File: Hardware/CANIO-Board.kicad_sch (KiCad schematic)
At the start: 52 parts, among them J1 DT13-2P, J2 Conn_01x04_Pin, J3 Conn_01x03_Pin, U1 STM32G0B1KETx, U2 AP63203WU-7, U3 AP63205WU-7, U4 ISOW1044, U5 TPS4H160AQPWPRQ1

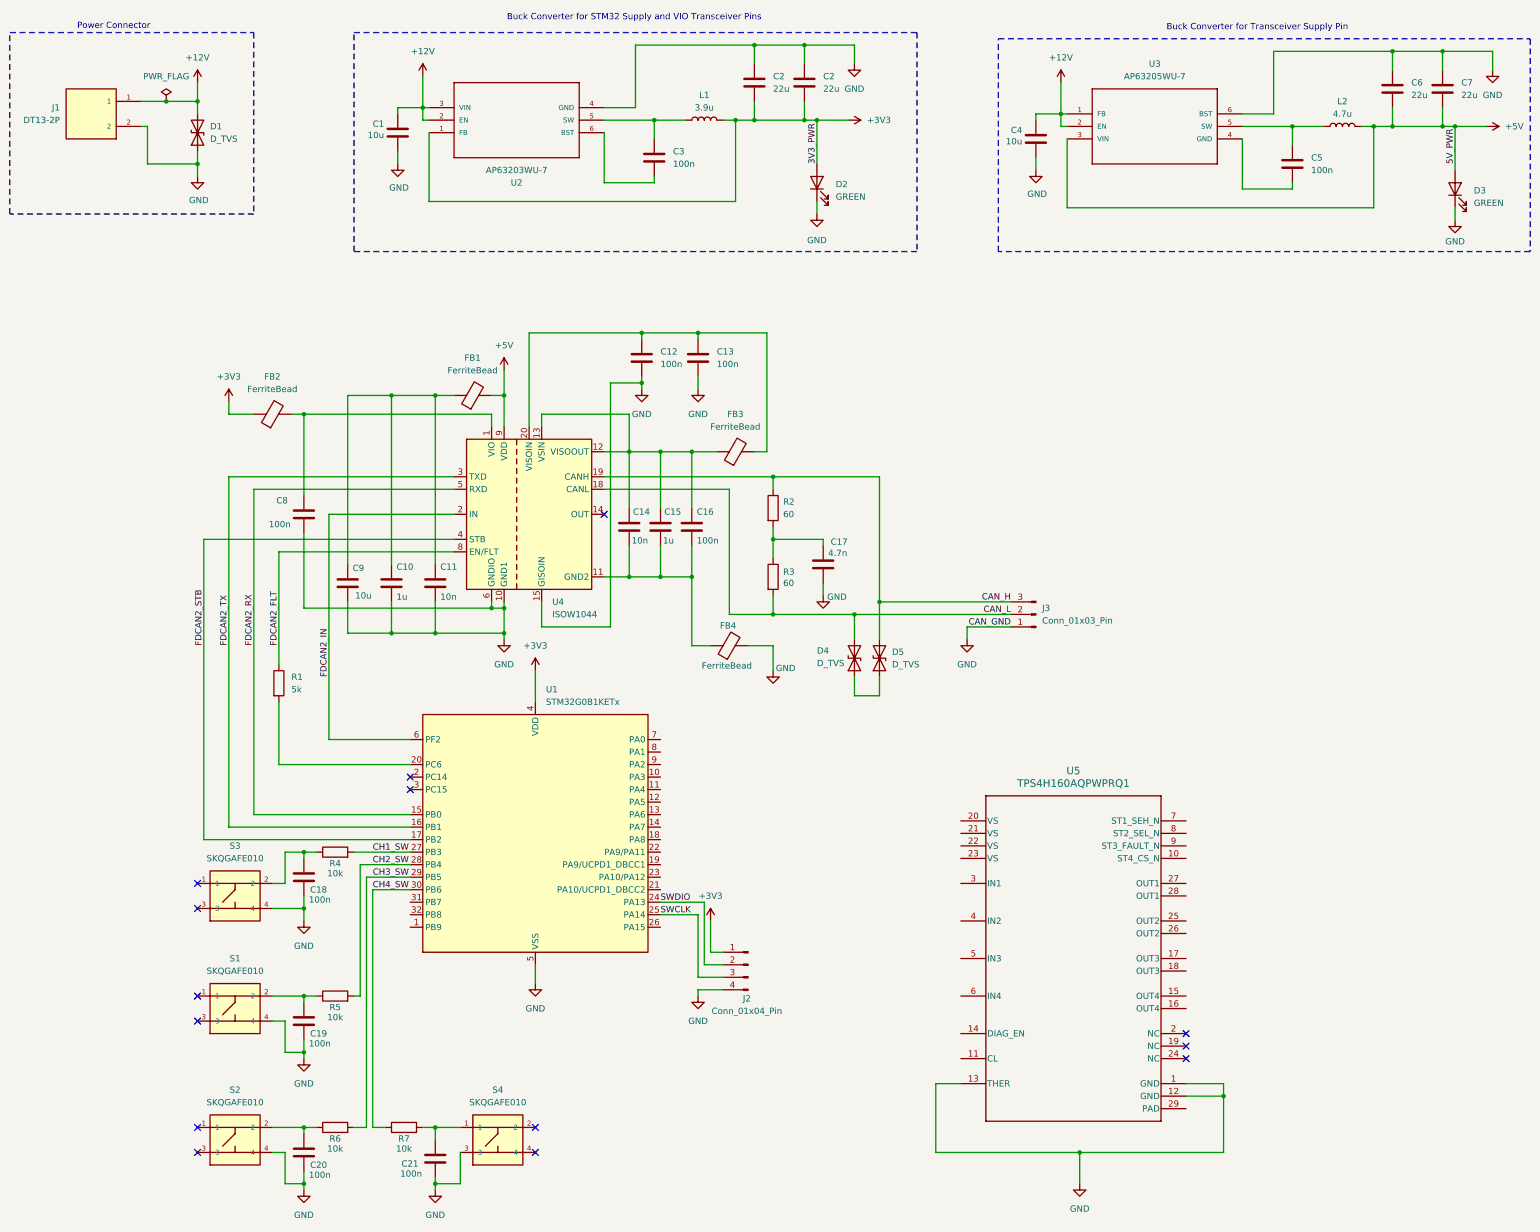
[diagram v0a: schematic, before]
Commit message: Restructured the schematic a little for modularity
- Gave each sub-component its own hierarchical sheet
- Placed the current schematic into a temporary sheet called 'old'.
  Gonna adapt everything and double check while doing so.
- Will make one commit with adapted schematic.
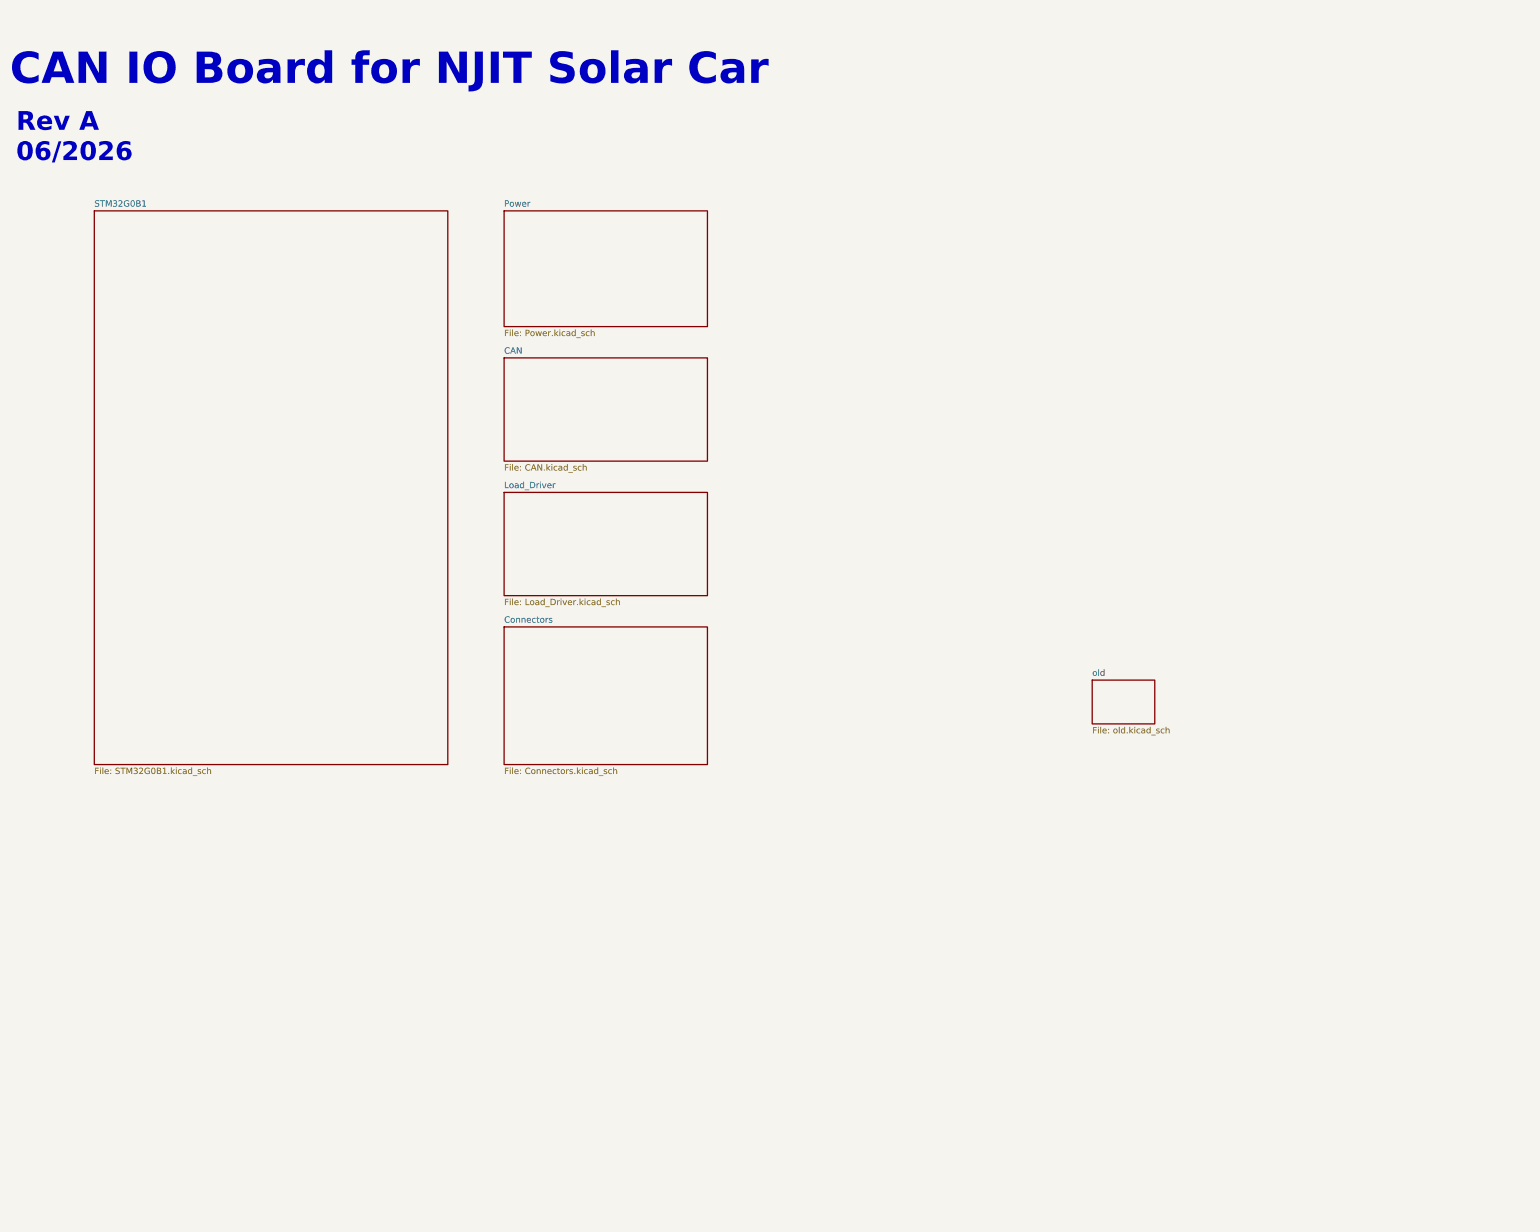
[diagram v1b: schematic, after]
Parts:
- removed C1, C4, C9: 10u, symbol Device:C
- removed C10, C15: 1u, symbol Device:C
- removed C11, C14: 10n, symbol Device:C
- removed C12, C13, C16, C18, C19, C20, C21, C3, C5, C8: 100n, symbol Device:C
- removed C17: 4.7n, symbol Device:C
- removed C2 (x2), C6, C7: 22u, symbol Device:C
- removed D1, D4, D5: D_TVS, symbol Device:D_TVS
- removed D2, D3: GREEN, symbol Device:LED
- removed FB1, FB2, FB3, FB4: FerriteBead, BLM15EX331SN1D:BEADC1005X55N, symbol Device:FerriteBead
- removed J1: DT13-2P, DT13-2P:TE_DT13-2P, symbol DT13-2P:DT13-2P
- removed J2: Conn_01x04_Pin, symbol Connector:Conn_01x04_Pin
- removed J3: Conn_01x03_Pin, symbol Connector:Conn_01x03_Pin
- removed L1: 3.9u, symbol Device:L
- removed L2: 4.7u, symbol Device:L
- removed R1: 5k, symbol Device:R
- removed R2, R3: 60, symbol Device:R
- removed R4, R5, R6, R7: 10k, symbol Device:R
- removed S1, S2, S3, S4: SKQGAFE010, SKQGAFE010:SW_SKQGAFE010, symbol SKQGAFE010:SKQGAFE010
- removed U1: STM32G0B1KETx, Package_QFP:LQFP-32_7x7mm_P0.8mm, symbol MCU_ST_STM32G0:STM32G0B1KETx
- removed U2: AP63203WU-7, AP63203WU-7:SOIC_05WU-7_DIO-M, symbol AP63203WU-7:AP63203WU-7
- removed U3: AP63205WU-7, AP63205WU-7:SOIC_05WU-7_DIO-M, symbol AP63205WU-7:AP63205WU-7
- removed U4: ISOW1044, Package_SO:SOIC-20W_7.5x12.8mm_P1.27mm, symbol Interface_CAN_LIN:ISOW1044
- removed U5: TPS4H160AQPWPRQ1, PWP0028C_N, symbol 2026-06-01_04-03-11:TPS4H160AQPWPRQ1
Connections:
- no-connect marks 14 -> 0
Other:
- added sheet CAN (CAN.kicad_sch)
- added sheet Connectors (Connectors.kicad_sch)
- added sheet Load_Driver (Load_Driver.kicad_sch)
- added sheet Power (Power.kicad_sch)
- added sheet STM32G0B1 (STM32G0B1.kicad_sch)
- added sheet old (old.kicad_sch)
- note added: "CAN IO Board for NJIT Solar Car"
- note added: "Rev A 06/2026"
- note removed: "Buck Converter for STM32 Supply and VIO Transceiver Pins"
- note removed: "Buck Converter for Transceiver Supply Pin"
- note removed: "Power Connector"
